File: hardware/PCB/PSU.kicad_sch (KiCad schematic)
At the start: 7 parts, among them IC7 AP2112K-3.3TRG1, T1 GSF2301

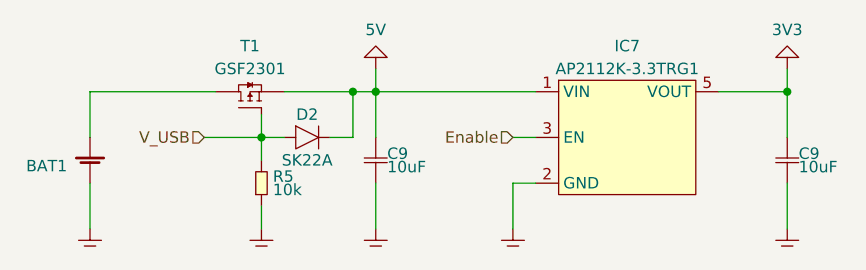
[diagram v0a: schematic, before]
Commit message: fixed the pcb being powered via ch340g
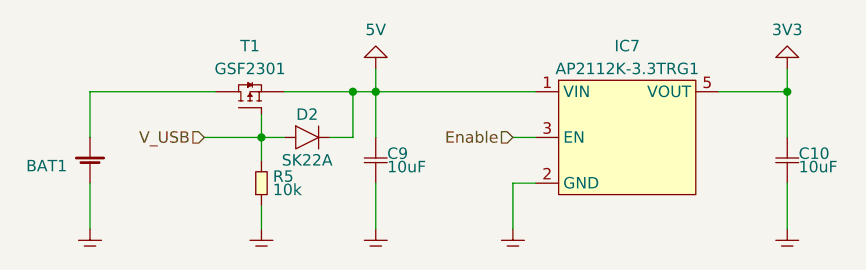
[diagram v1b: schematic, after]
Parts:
- renumbered C9 to C10
